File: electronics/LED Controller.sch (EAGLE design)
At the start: 20 parts, among them J1 1-770968-0, J2 DF1BZ-8DP-2.5DSA, J3 LED8, J4 LED16, U1 MCP23S08-E/SO, U2 ATMEGA328PB32-TQFP, U3 MCP23S17T-E/SO

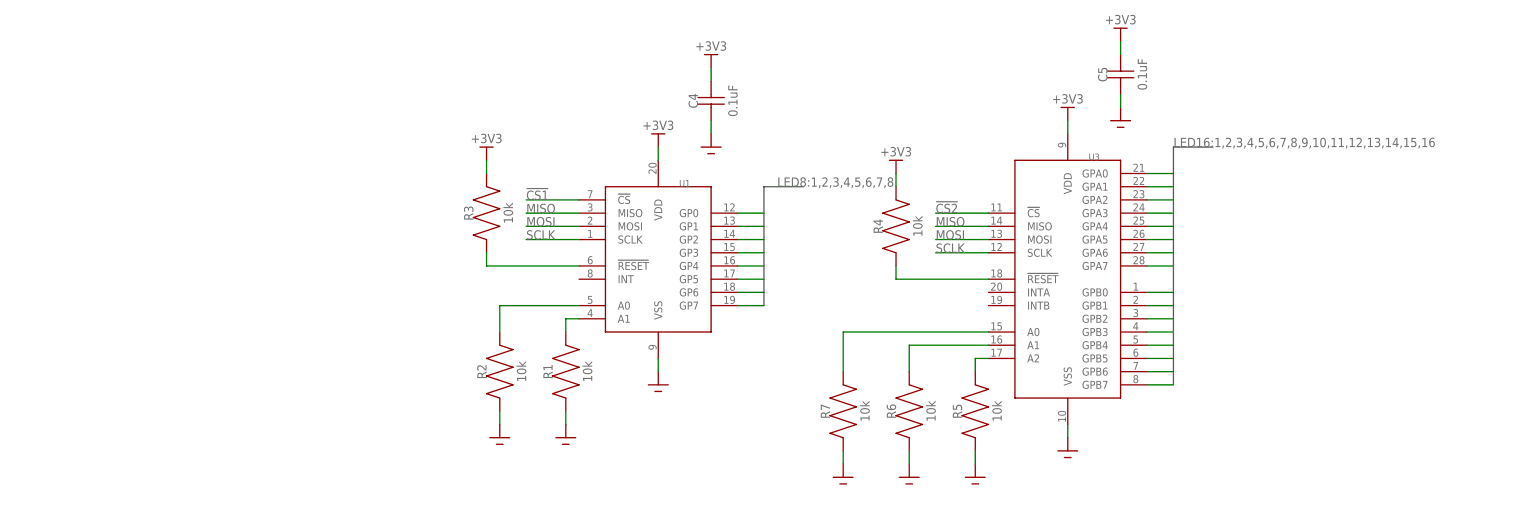
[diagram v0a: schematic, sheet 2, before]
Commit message: Added current-limiting resistors for LEDs
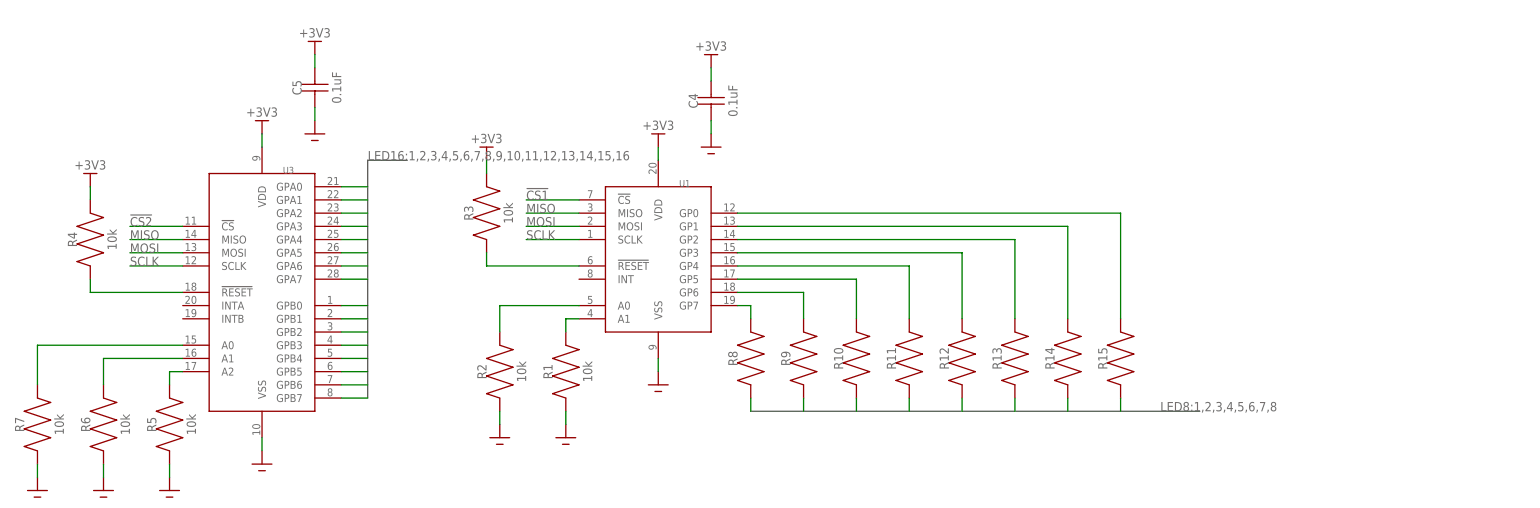
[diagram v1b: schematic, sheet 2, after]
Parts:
- added R10, R11, R12, R13, R14, R15, R8, R9: (no value), Zach:RESISTOR0805
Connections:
- new net N$10: R10.P$2, U1.GP5
- new net N$11: R11.P$2, U1.GP4
- new net N$12: R12.P$2, U1.GP3
- new net N$13: R13.P$2, U1.GP2
- new net N$14: R14.P$2, U1.GP1
- new net N$15: R15.P$2, U1.GP0
- new net N$8: R8.P$2, U1.GP7
- new net N$9: R9.P$2, U1.GP6
- net A: now also R15.P$1; no longer U1.GP0
- net B: now also R14.P$1; no longer U1.GP1
- net C: now also R13.P$1; no longer U1.GP2
- net D: now also R12.P$1; no longer U1.GP3
- net E: now also R11.P$1; no longer U1.GP4
- net F: now also R10.P$1; no longer U1.GP5
- net G: now also R9.P$1; no longer U1.GP6
- net H: now also R8.P$1; no longer U1.GP7
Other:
- moved on the sheet: C5, R4, R5, R6, R7, U3

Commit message: Added pull-up on RESET
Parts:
- added R16: 10k, Zach:RESISTOR0805
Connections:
- net !RESET: now also R16.P$1
- net +3V3: now also R16.P$2
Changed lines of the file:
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@@
 <part name="R14" library="Zach" deviceset="RESISTOR" device="0805"/>
 <part name="R15" library="Zach" deviceset="RESISTOR" device="0805"/>
+<part name="R16" library="Zach" deviceset="RESISTOR" device="0805" value="10k"/>
+<part name="P+11" library="Zach" deviceset="+3V3" device=""/>
 </parts>
 <sheets>
@@
 <instance part="GND14" gate="1" x="106.68" y="-30.48" smashed="yes"/>
 <instance part="GND15" gate="1" x="124.46" y="-30.48" smashed="yes"/>
+<instance part="R16" gate="G$1" x="33.02" y="-15.24" smashed="yes" rot="R90">
+<attribute name="NAME" x="30.48" y="-7.62" size="1.778" layer="95" rot="R90" align="bottom-center"/>
+<attribute name="VALUE" x="38.1" y="-7.62" size="1.778" layer="96" rot="R90" align="bottom-center"/>
+</instance>
+<instance part="P+11" gate="G$1" x="33.02" y="5.08" smashed="yes">
+<attribute name="VALUE" x="33.02" y="7.62" size="1.778" layer="96" rot="R180" align="bottom-center"/>
+</instance>
 </instances>
 <busses>
@@
 <wire x1="139.7" y1="2.54" x2="142.24" y2="2.54" width="0.1524" layer="91"/>
 </segment>
+<segment>
+<pinref part="R16" gate="G$1" pin="P$2"/>
+<pinref part="P+11" gate="G$1" pin="+3V3"/>
+<wire x1="33.02" y1="2.54" x2="33.02" y2="0" width="0.1524" layer="91"/>
+</segment>
 </net>
 <net name="GND" class="0">
@@
 <segment>
 <pinref part="U2" gate="G$1" pin="PC6"/>
-<wire x1="53.34" y1="-17.78" x2="40.64" y2="-17.78" width="0.1524" layer="91"/>
+<wire x1="53.34" y1="-17.78" x2="33.02" y2="-17.78" width="0.1524" layer="91"/>
 <label x="40.64" y="-17.78" size="1.778" layer="95"/>
-</segment>
-</net>
+<pinref part="R16" gate="G$1" pin="P$1"/>
+<wire x1="33.02" y1="-17.78" x2="33.02" y2="-15.24" width="0.1524" layer="91"/>
+</segment>
+</net>
